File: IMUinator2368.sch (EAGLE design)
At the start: 73 parts, among them J001 USB_MICROB_JST, J003 UP501, J301 JST 2mm, J401 M06, J701 MICROSD-SOCKET, Q050 PMOS, Q201 PMOS, U2 BMP180, U201 5319, U301 73831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

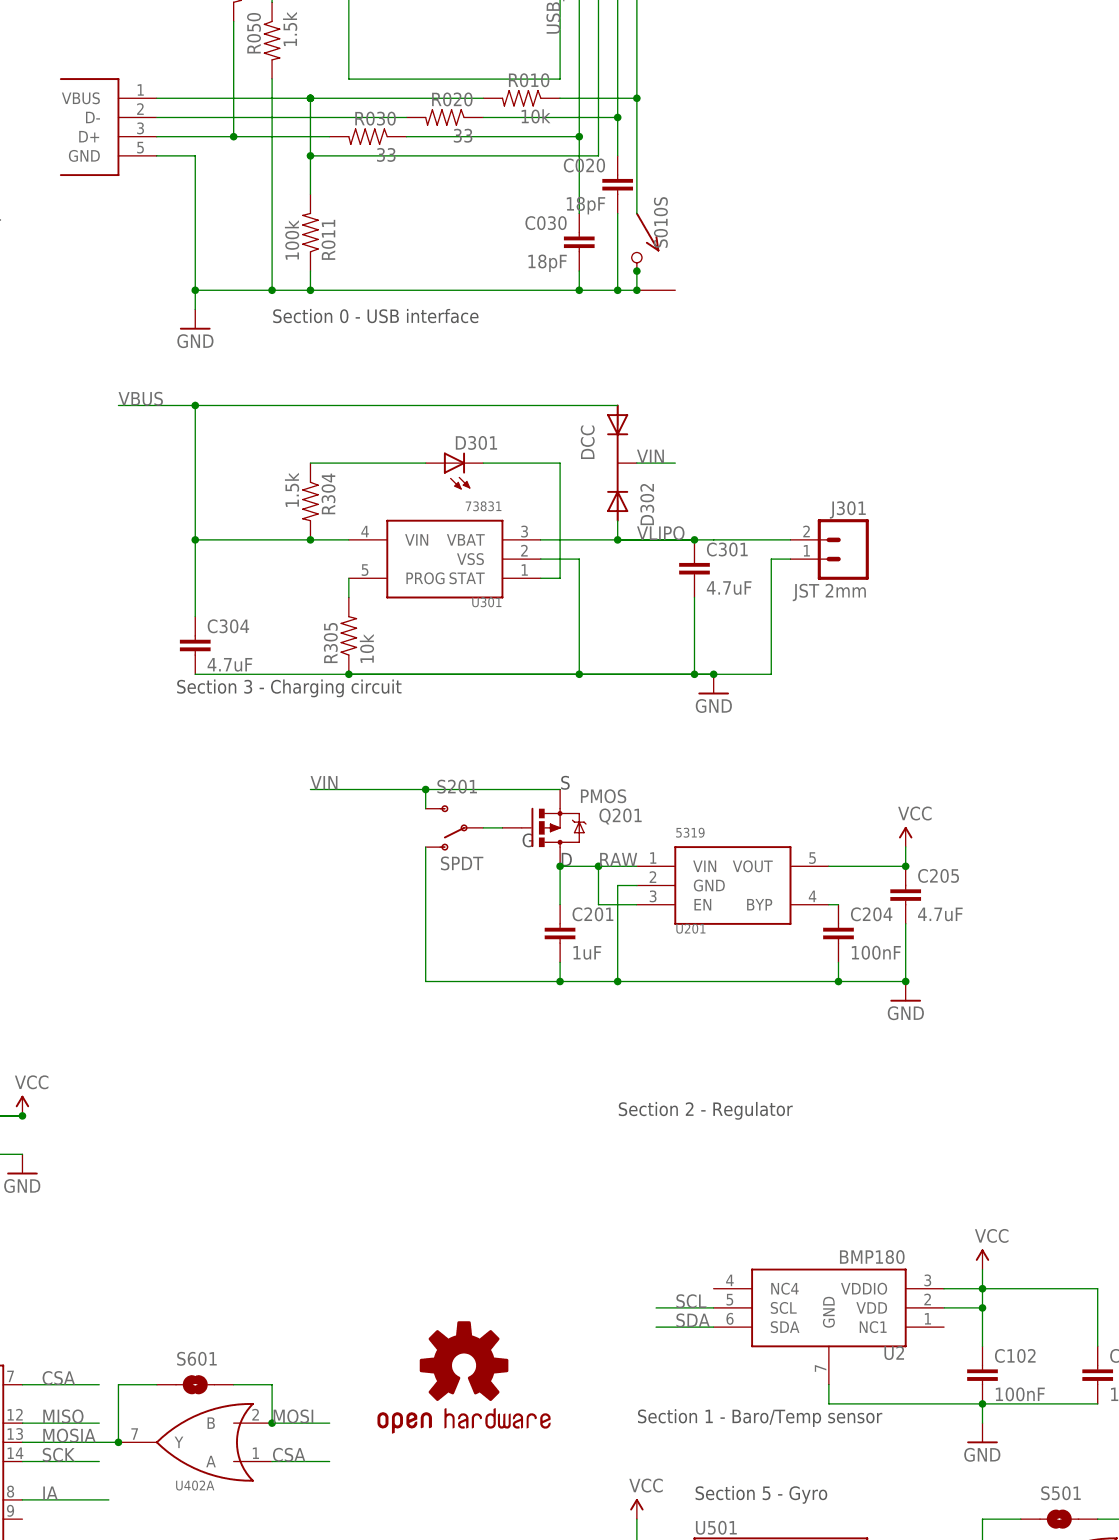
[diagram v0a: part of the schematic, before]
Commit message: Merged Mio's KwanSystems.lbr, updated all eagle files to use it.
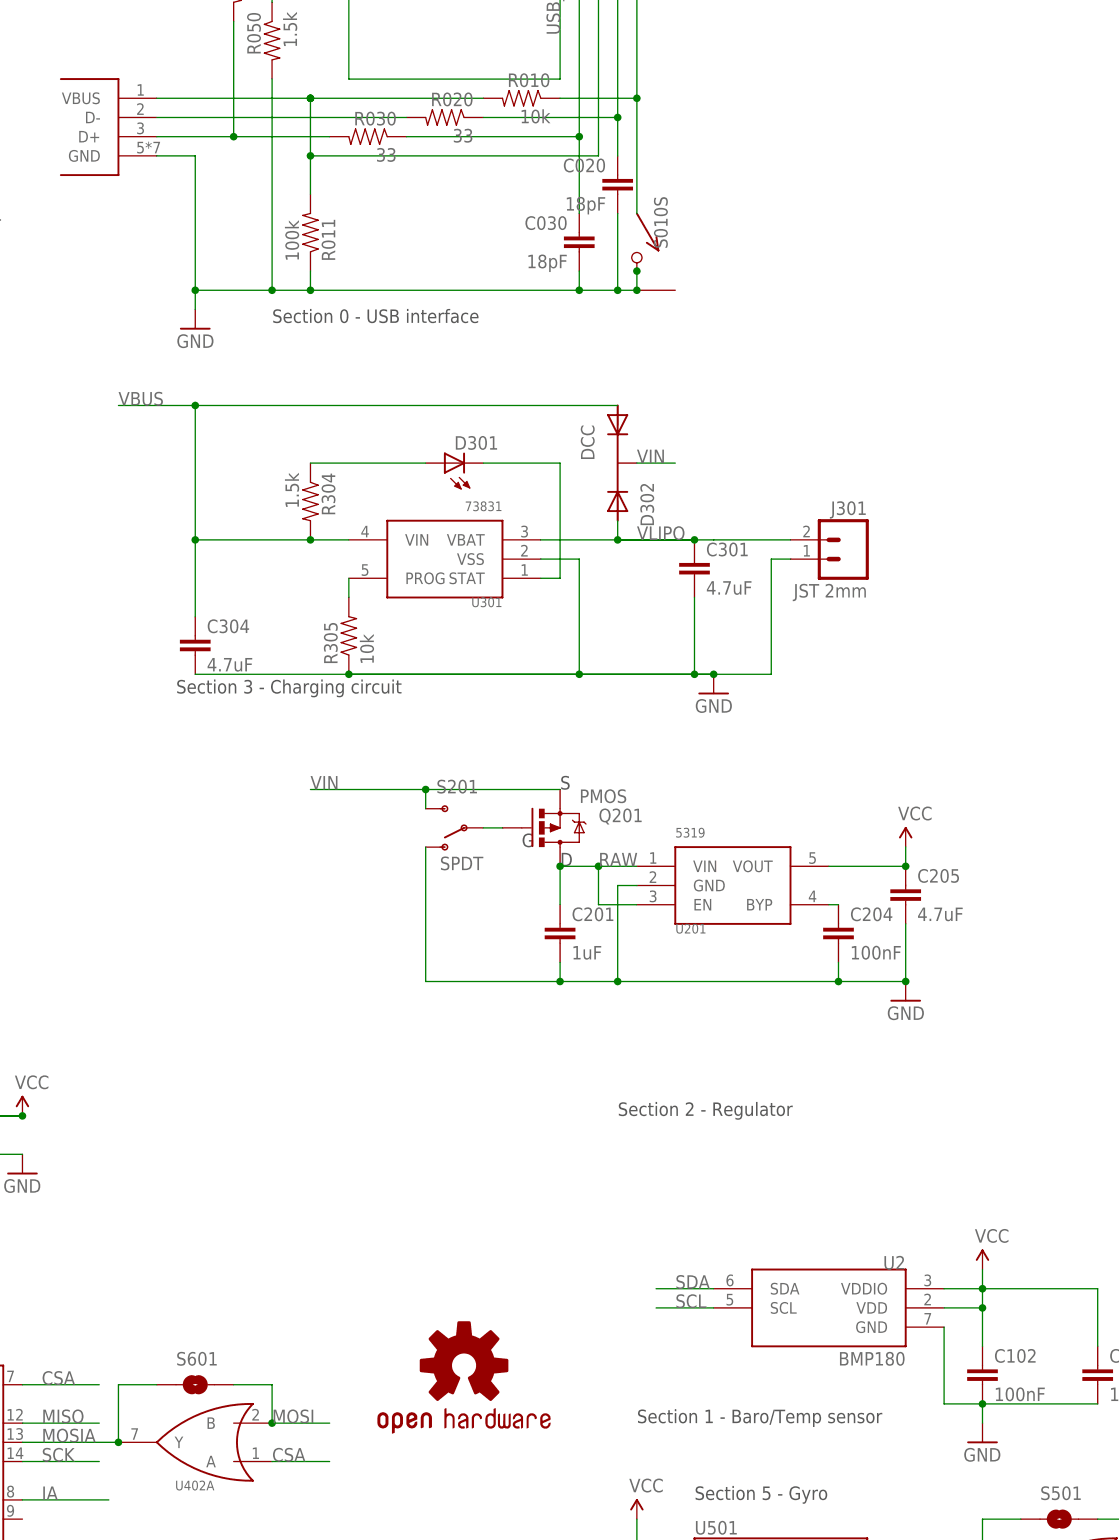
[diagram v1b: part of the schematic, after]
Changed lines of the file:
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@@
 <?xml version="1.0" encoding="utf-8"?>
 <!DOCTYPE eagle SYSTEM "eagle.dtd">
-<eagle version="6.1">
+<eagle version="6.2">
 <drawing>
 <settings>
@@
 <instance part="GND18" gate="1" x="-33.02" y="25.4" rot="MR0"/>
 <instance part="P+15" gate="1" x="-17.78" y="35.56" rot="MR0"/>
-<instance part="U2" gate="G$1" x="53.34" y="111.76" rot="R180">
-<attribute name="DIGIKEY" value="828-1027-1-ND" x="53.34" y="111.76" size="1.778" layer="96" display="off"/>
+<instance part="U2" gate="G$1" x="53.34" y="111.76" rot="MR0">
+<attribute name="DIGIKEY" value="828-1027-1-ND" x="53.34" y="111.76" size="1.778" layer="96" rot="MR180" display="off"/>
 </instance>
 <instance part="C103" gate="G$1" x="88.9" y="101.6">
@@
 <segment>
 <wire x1="73.66" y1="99.06" x2="73.66" y2="96.52" width="0.1524" layer="91"/>
-<wire x1="53.34" y1="101.6" x2="53.34" y2="99.06" width="0.1524" layer="91"/>
-<wire x1="53.34" y1="99.06" x2="73.66" y2="99.06" width="0.1524" layer="91"/>
+<wire x1="68.58" y1="109.22" x2="68.58" y2="99.06" width="0.1524" layer="91"/>
+<wire x1="68.58" y1="99.06" x2="73.66" y2="99.06" width="0.1524" layer="91"/>
 <wire x1="73.66" y1="99.06" x2="88.9" y2="99.06" width="0.1524" layer="91"/>
 <junction x="73.66" y="99.06"/>
@@
 </segment>
 <segment>
-<wire x1="30.48" y1="109.22" x2="38.1" y2="109.22" width="0.1524" layer="91"/>
-<label x="33.02" y="109.22" size="1.778" layer="95"/>
+<wire x1="30.48" y1="114.3" x2="38.1" y2="114.3" width="0.1524" layer="91"/>
+<label x="33.02" y="114.3" size="1.778" layer="95"/>
 <pinref part="U2" gate="G$1" pin="SDA"/>
 </segment>
